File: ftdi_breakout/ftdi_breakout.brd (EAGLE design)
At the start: 59.4 x 33 mm, 16 parts, among them U1 FT231XS

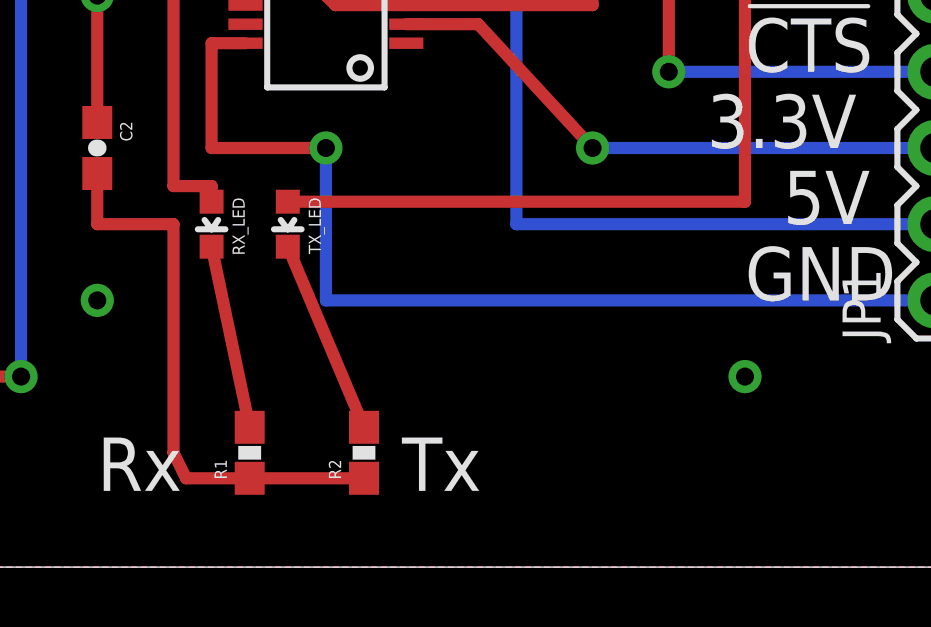
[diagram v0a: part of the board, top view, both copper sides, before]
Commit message: Modified to connect the chip as sinking the current from LED.
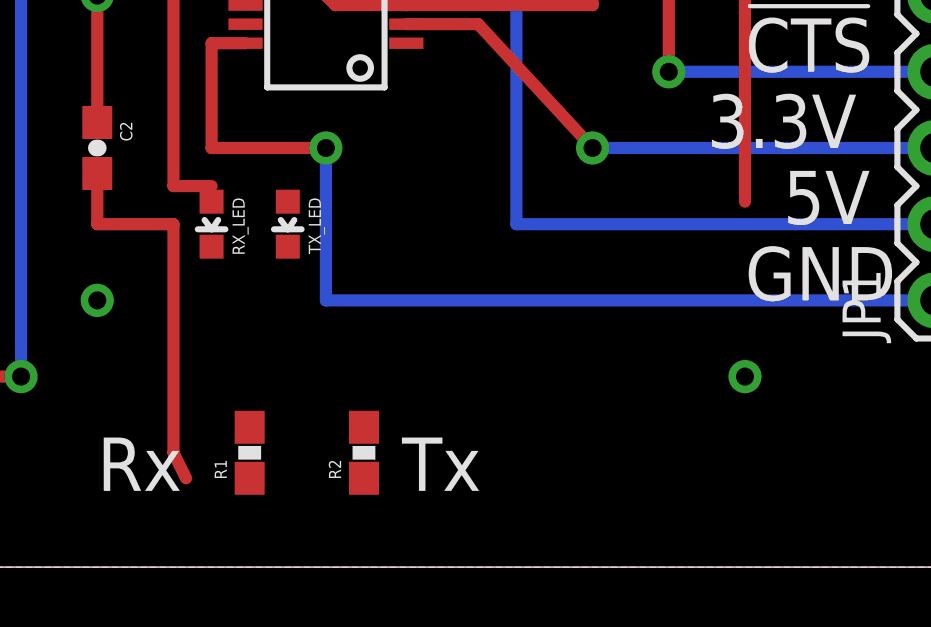
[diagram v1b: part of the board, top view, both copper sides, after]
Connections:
- net 5V: now also R1.1, R2.1
- net GND: no longer R1.1, R2.1
- net N$4: now also RX_LED.C; no longer RX_LED.A
- net N$5: now also TX_LED.C; no longer TX_LED.A
- net N$6: now also TX_LED.A; no longer TX_LED.C
- net N$7: now also RX_LED.A; no longer RX_LED.C
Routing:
- net N$5: track 37.5 -> 22.3 mm
- net N$6: track 6.53 -> 0.00 mm
- net N$7: track 6.15 -> 0.00 mm
- net GND: track 19.1 -> 13.2 mm
- net N$4: track 10.9 -> 10.3 mm
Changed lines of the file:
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@@
 <wire x1="53.34" y1="57.15" x2="53.34" y2="48.26" width="0.4064" layer="1"/>
 <wire x1="53.34" y1="48.26" x2="58.42" y2="48.26" width="0.4064" layer="1"/>
+<contactref element="R2" pad="1"/>
+<contactref element="R1" pad="1"/>
+<wire x1="35.56" y1="29.63" x2="39.37" y2="29.63" width="0" layer="19" extent="1-1"/>
+<wire x1="35.4203" y1="47.3075" x2="35.56" y2="29.63" width="0" layer="19" extent="1-1"/>
 </signal>
 <signal name="3.3V">
@@
 <wire x1="35.4203" y1="47.9425" x2="35.4203" y2="48.5775" width="0.4064" layer="1"/>
 </signal>
-<signal name="N$6">
-<contactref element="TX_LED" pad="C"/>
-<contactref element="R2" pad="2"/>
-<wire x1="39.37" y1="31.33" x2="36.83" y2="37.35" width="0.4064" layer="1"/>
-</signal>
-<signal name="N$7">
-<contactref element="RX_LED" pad="C"/>
-<contactref element="R1" pad="2"/>
-<wire x1="35.56" y1="31.33" x2="34.29" y2="37.35" width="0.4064" layer="1"/>
-</signal>
 <signal name="GND">
 <contactref element="C1" pad="2"/>
@@
 <contactref element="U1" pad="6"/>
 <contactref element="U1" pad="16"/>
-<contactref element="R2" pad="1"/>
-<contactref element="R1" pad="1"/>
 <contactref element="JP1" pad="7"/>
 <contactref element="JP3" pad="GND"/>
-<wire x1="35.56" y1="29.63" x2="39.37" y2="29.63" width="0.4064" layer="1"/>
 <polygon width="0.4064" layer="1" isolate="0.3048">
 <vertex x="64.77" y="26.67"/>
@@
 <wire x1="33.02" y1="38.1" x2="33.02" y2="30.48" width="0.4064" layer="1"/>
 <wire x1="33.02" y1="30.48" x2="33.44" y2="29.63" width="0.4064" layer="1"/>
-<wire x1="33.44" y1="29.63" x2="35.56" y2="29.63" width="0.4064" layer="1"/>
+<wire x1="40.7797" y1="47.3075" x2="58.42" y2="50.8" width="0" layer="19" extent="1-1"/>
 <wire x1="35.4203" y1="46.6725" x2="40.7797" y2="47.3075" width="0" layer="19" extent="1-1"/>
 <wire x1="30.48" y1="39.79" x2="35.4203" y2="46.6725" width="0" layer="19" extent="1-1"/>
+<wire x1="30.48" y1="35.56" x2="30.48" y2="38.1" width="0" layer="19" extent="1-1"/>
+<wire x1="22.86" y1="40.51" x2="30.48" y2="39.79" width="0" layer="19" extent="1-1"/>
+<wire x1="19.05" y1="41.06" x2="22.86" y2="40.51" width="0" layer="19" extent="1-1"/>
+<wire x1="12.66" y1="41.58" x2="19.05" y2="41.06" width="0" layer="19" extent="1-1"/>
+<wire x1="52.07" y1="33.02" x2="40.7797" y2="47.3075" width="0" layer="19" extent="1-1"/>
 </signal>
 <signal name="TXO">
@@
 <signal name="N$5">
 <contactref element="U1" pad="10"/>
-<contactref element="TX_LED" pad="A"/>
 <wire x1="52.07" y1="49.8475" x2="52.07" y2="38.85" width="0.4064" layer="1"/>
-<wire x1="52.07" y1="38.85" x2="36.83" y2="38.85" width="0.4064" layer="1"/>
 <wire x1="40.7797" y1="49.8475" x2="52.07" y2="49.8475" width="0.4064" layer="1"/>
+<contactref element="TX_LED" pad="C"/>
+<wire x1="36.83" y1="37.35" x2="40.7797" y2="49.8475" width="0" layer="19" extent="1-1"/>
 </signal>
 <signal name="N$4">
 <contactref element="U1" pad="17"/>
-<contactref element="RX_LED" pad="A"/>
 <wire x1="35.4203" y1="46.0375" x2="33.02" y2="46.0375" width="0.4064" layer="1"/>
 <wire x1="33.02" y1="46.0375" x2="33.02" y2="39.37" width="0.4064" layer="1"/>
 <wire x1="33.02" y1="39.37" x2="34.29" y2="39.37" width="0.4064" layer="1"/>
-<wire x1="34.29" y1="39.37" x2="34.29" y2="38.85" width="0.4064" layer="1"/>
+<contactref element="RX_LED" pad="C"/>
+<wire x1="34.29" y1="37.35" x2="34.29" y2="39.37" width="0" layer="19" extent="1-1"/>
 </signal>
 <signal name="N$1">
@@
 <signal name="N$14">
 </signal>
+<signal name="N$6">
+<contactref element="R2" pad="2"/>
+<contactref element="TX_LED" pad="A"/>
+<wire x1="39.37" y1="31.33" x2="36.83" y2="38.85" width="0" layer="19" extent="1-1"/>
+</signal>
+<signal name="N$7">
+<contactref element="R1" pad="2"/>
+<contactref element="RX_LED" pad="A"/>
+<wire x1="35.56" y1="31.33" x2="34.29" y2="38.85" width="0" layer="19" extent="1-1"/>
+</signal>
 </signals>

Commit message: Modified layout file.
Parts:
- moved R1 5.24 mm to (34.3, 35.6)
- moved R2 5.08 mm to (39.4, 35.6)
- moved TX_LED 2.84 mm to (39.4, 39.4), turned to 0 degrees
- moved C1 1.27 mm to (20.3, 41.9)
- moved RX_LED 1.27 mm to (34.3, 39.4), turned to 0 degrees
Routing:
- net GND: track 13.2 -> 54.1 mm, vias 2 -> 4
- net N$5: track 22.3 -> 54.1 mm
- net 5V: track 74.8 -> 96.1 mm
- net !CTS: track 23.7 -> 30.3 mm
- net TXO: track 33.8 -> 30.3 mm
- net N$3: track 58.2 -> 54.7 mm
- net N$4: track 10.3 -> 7.05 mm
- net N$7: track 0.00 -> 2.21 mm
- net N$6: track 0.00 -> 2.21 mm
- net !RTS: track 19.4 -> 21.6 mm
- net N$1: track 62.1 -> 60.6 mm
- net N$2: track 9.72 -> 10.5 mm
- net RXI: track 26.7 -> 26.0 mm
